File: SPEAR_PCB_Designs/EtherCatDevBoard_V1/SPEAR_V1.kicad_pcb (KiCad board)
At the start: 4 copper layers, 44 x 55 mm, 105 parts, among them J1 USB_C_Receptacle_USB2.0_16P, J2 FTSH-107-01-F-DV-K-P-TR, J3 Conn_01x21_Pin, J4 Conn_01x21_Pin, J5 SM04B-GHS-TB, J6 SM04B-GHS-TB, SW1 SW_Push, T1 H1102NLT, T2 H1102NLT, U1 USBLC6-2SC6, U2 STM32F446RCT6, U3 AMS1117-3.3, U4 LAN9252I/ML, U5 24FC512-I/SN, Y1 16MHz, Y2 25MHz

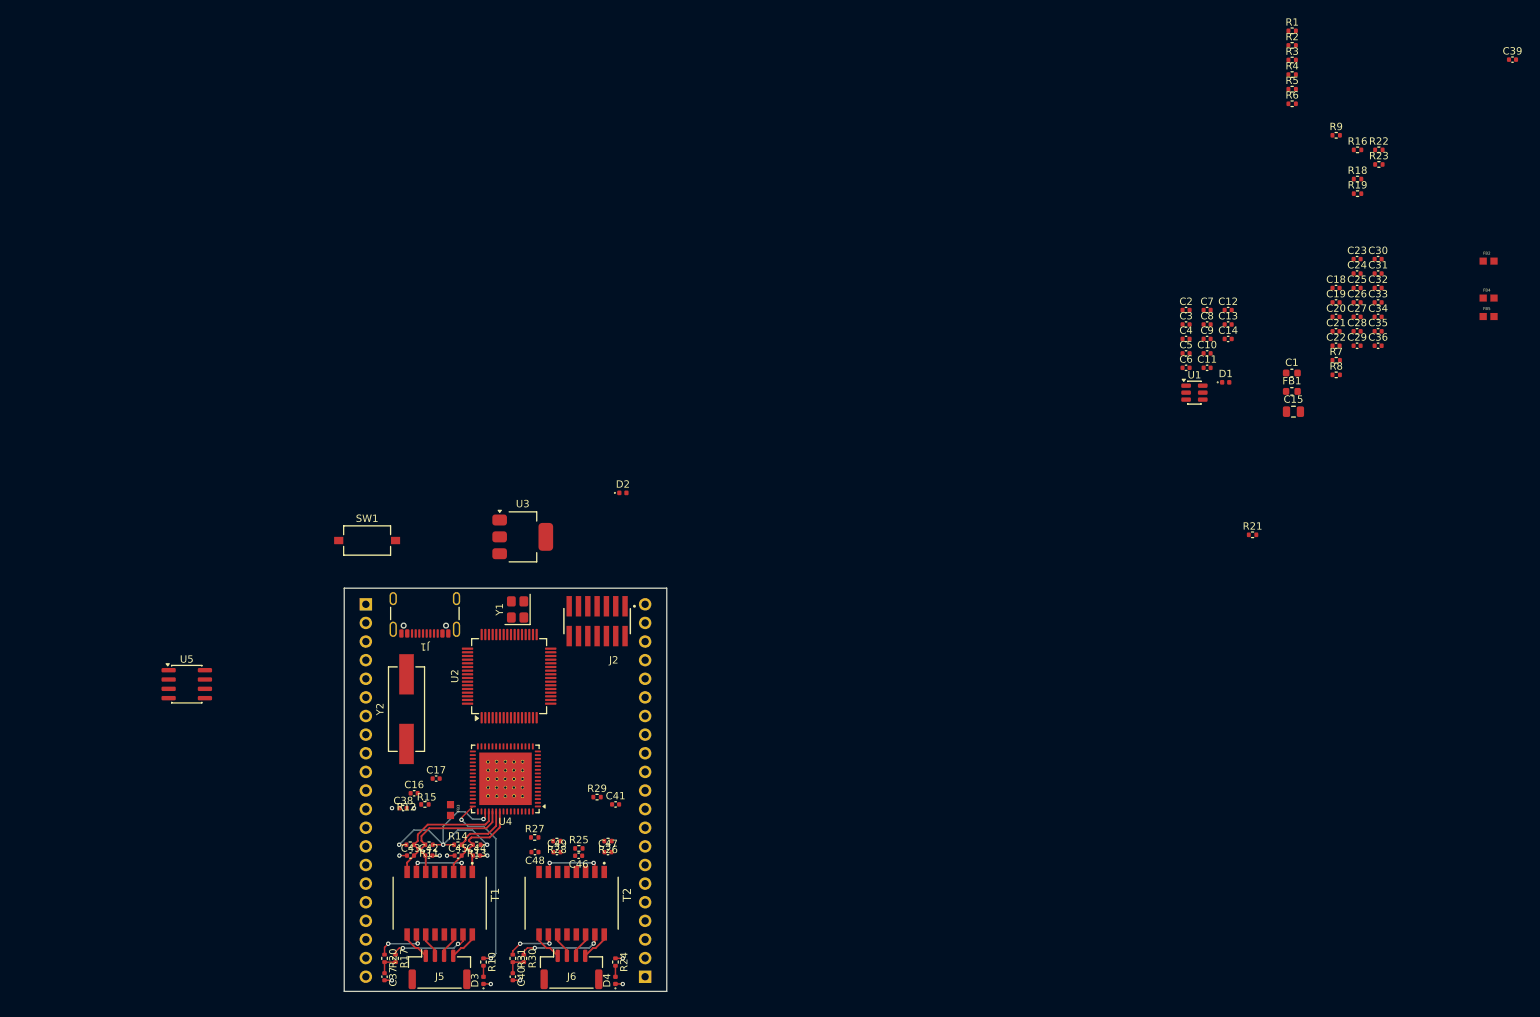
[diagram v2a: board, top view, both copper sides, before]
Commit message: Henry's continued work on the EtherCAT microcontroller dev. board.
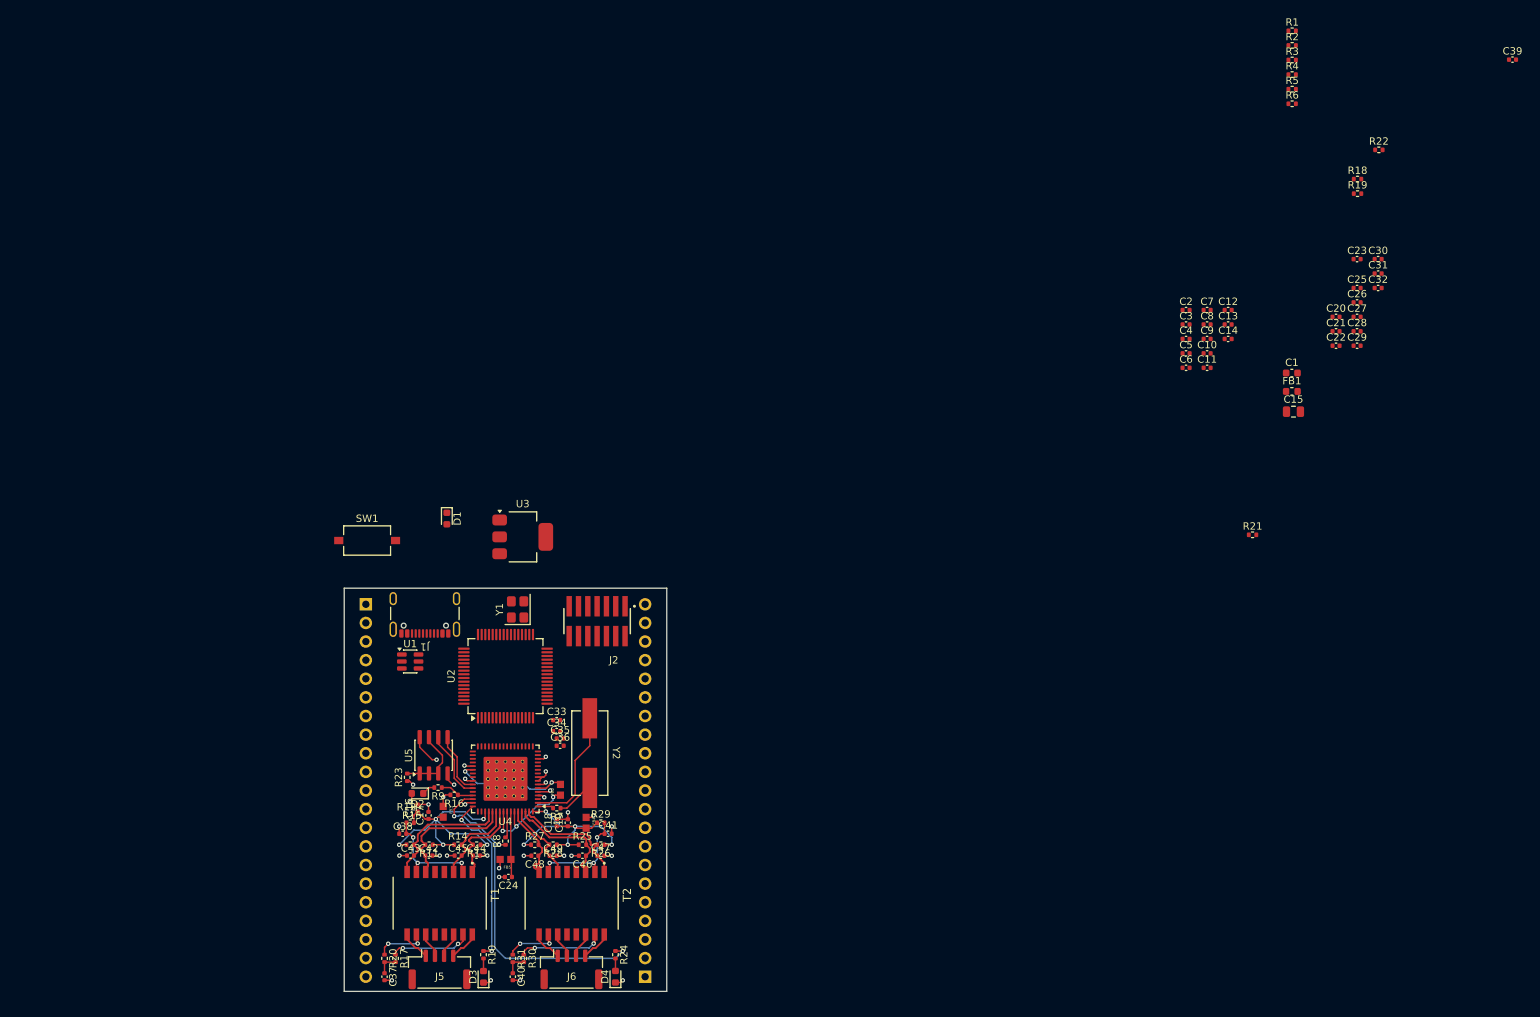
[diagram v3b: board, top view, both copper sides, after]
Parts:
- D1, D2, D3, D4: footprint LED_SMD:LED_0402_1005Metric -> LED_SMD:LED_0603_1608Metric
- moved R23 156.7 mm to (86.6, 127.8), turned to 90 degrees
- moved FB5 153.2 mm to (100.0, 139.0), turned to 180 degrees
- moved R9 151.4 mm to (90.8, 129.2), turned to 180 degrees
- moved R16 151.4 mm to (93.0, 130.2), turned to 180 degrees
- moved FB2 145.7 mm to (107.5, 129.5), turned to 90 degrees
- moved FB4 142.4 mm to (111.0, 134.0), turned to -90 degrees
- moved C24 142.1 mm to (100.4, 141.4), turned to 180 degrees
- moved R8 129.9 mm to (100.0, 136.5), turned to 90 degrees
- moved C18 128.9 mm to (107.0, 134.0), turned to 90 degrees
- moved C19 126.6 mm to (108.5, 134.0), turned to 90 degrees
- moved C33 125.7 mm to (107.0, 120.0)
- moved C34 125.5 mm to (107.0, 121.5)
- moved C35 124.6 mm to (107.5, 122.5)
- moved C36 124.2 mm to (107.5, 123.5)
- moved R7 122.6 mm to (107.0, 132.0), turned to 180 degrees
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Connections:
- C16 pad 2: Net-(C16-Pad2) -> GND
- C17 pad 2: Net-(C16-Pad2) -> GND
- C18 pad 2: Net-(C18-Pad2) -> GND
- C19 pad 2: Net-(C18-Pad2) -> GND
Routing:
- net /LAN9252/GPIO1: track 1.00 -> 45.0 mm, vias 1 -> 2
- net /LAN9252/VDD33TXRX2: track 0.00 -> 33.1 mm, vias 0 -> 5
- net GND: track 8.11 -> 29.2 mm, vias 9 -> 23
- net /LAN9252/VDDCR: track 0.00 -> 17.9 mm, vias 0 -> 2
- net +3.3V: track 0.00 -> 16.9 mm, vias 0 -> 10
- net Net-(U4-OSCO): track 0.00 -> 16.8 mm
- net /LAN9252/TXB_N: track 0.00 -> 16.4 mm
- net /LAN9252/TXB_P: track 0.00 -> 15.8 mm
- net /LAN9252/VDD12TX1: track 0.00 -> 15.0 mm, vias 0 -> 3
- net /LAN9252/RXB_N: track 0.00 -> 10.9 mm
- net /LAN9252/RXB_P: track 0.00 -> 10.8 mm
- net Net-(U5-A0): track 0.00 -> 10.2 mm
- net /LAN9252/I2C_SCL: track 0.00 -> 9.59 mm
- net Net-(U4-VDD33BIAS): track 0.00 -> 9.00 mm
- net /LAN9252/I2C_SDL: track 0.00 -> 8.52 mm
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
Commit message: Continued work on the pcb layout of the EtherCAT uC dev board. Updated schematic to use a power mux.
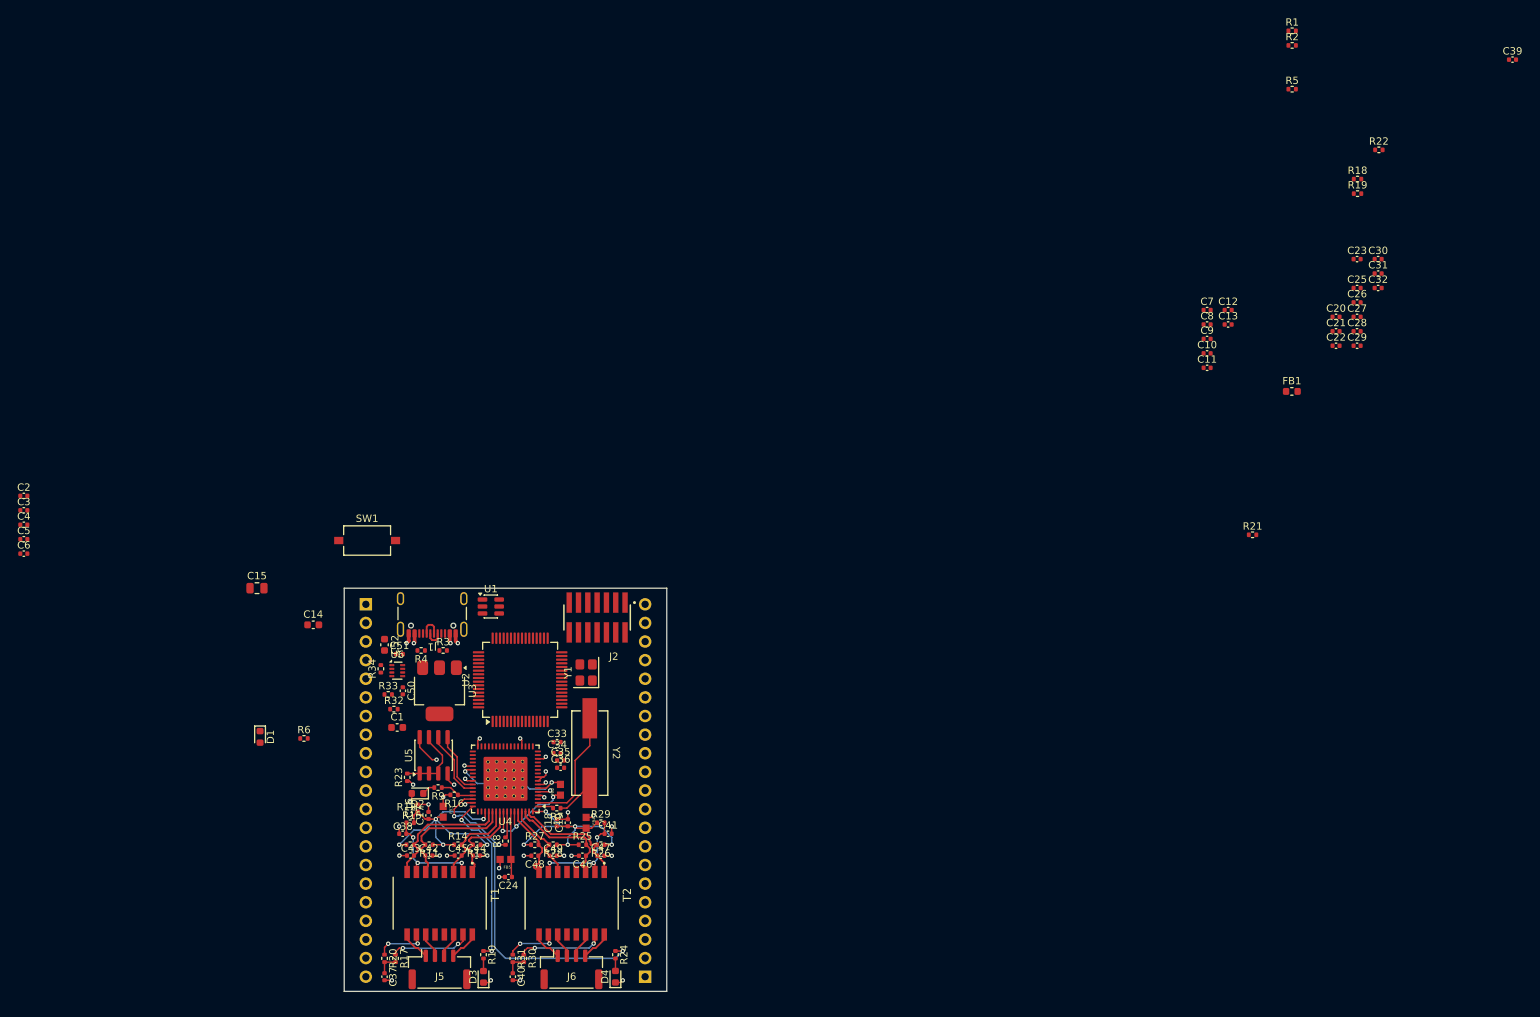
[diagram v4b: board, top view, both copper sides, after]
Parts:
- added C50: 1u, Capacitor_SMD:C_0402_1005Metric, F.Cu at (86.0, 116.0)
- added C51: 1u, Capacitor_SMD:C_0402_1005Metric, F.Cu at (85.5, 111.0)
- added C52: 10u, Capacitor_SMD:C_0603_1608Metric, F.Cu at (83.5, 109.7)
- added R32: 7.5k, Resistor_SMD:R_0402_1005Metric, F.Cu at (84.8, 118.5)
- added R33: 5.1k, Resistor_SMD:R_0402_1005Metric, F.Cu at (84.0, 116.5)
- added R34: 10k, Resistor_SMD:R_0402_1005Metric, F.Cu at (83.0, 113.0)
- added U6: TPS2116DRL, Package_TO_SOT_SMD:SOT-583-8, F.Cu at (85.2, 113.2)
- C14: footprint Capacitor_SMD:C_0402_1005Metric -> Capacitor_SMD:C_0603_1608Metric
- moved C2 160.6 mm to (34.3, 89.4)
- moved C3 160.6 mm to (34.3, 91.4)
- moved C4 160.6 mm to (34.3, 93.3)
- moved C5 160.6 mm to (34.3, 95.3)
- moved C6 160.6 mm to (34.3, 97.3)
- moved R6 160.2 mm to (72.5, 122.5)
- moved C15 143.4 mm to (66.1, 102.0)
- moved R4 142.4 mm to (88.5, 110.5), turned to 180 degrees
- moved R3 141.1 mm to (91.5, 110.5)
- moved C1 131.3 mm to (85.2, 121.0)
- moved C14 130.8 mm to (73.8, 107.0)
- moved D1 39.2 mm to (66.5, 122.3)
- moved U3 23.9 mm to (91.0, 116.0), turned to -90 degrees
- moved U1 13.3 mm to (98.0, 104.5)
- moved Y1 12.7 mm to (111.0, 113.5)
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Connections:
- C15 pad 1: +3.3V -> /STM32F446RC/3.3V_USB
- J3 pad 1: +3.3V -> /STM32F446RC/PC0
- J3 pad 10: /STM32F446RC/PA1 -> /STM32F446RC/PB0
- J3 pad 11: /STM32F446RC/PA4 -> /STM32F446RC/PB1
- J3 pad 12: /STM32F446RC/PC4 -> /STM32F446RC/PB2
- J3 pad 13: /STM32F446RC/PC5 -> /STM32F446RC/PB10
- J3 pad 14: /STM32F446RC/PB0 -> /STM32F446RC/PB12
- J3 pad 15: /STM32F446RC/PB1 -> /STM32F446RC/PB13
- J3 pad 16: /STM32F446RC/PB2 -> /STM32F446RC/PB14
- J3 pad 17: /STM32F446RC/PB10 -> /STM32F446RC/PB15
- J3 pad 18: /STM32F446RC/PB12 -> /STM32F446RC/PC9
- J3 pad 19: /STM32F446RC/PB13 -> /STM32F446RC/PC8
- J3 pad 2: +3.3V -> /STM32F446RC/PC1
- J3 pad 20: /STM32F446RC/PB14 -> /STM32F446RC/PC7
- J3 pad 21: /STM32F446RC/PB15 -> /STM32F446RC/PC6
- J3 pad 3: GND -> /STM32F446RC/PC2
- J3 pad 4: GND -> /STM32F446RC/PC3
- J3 pad 5: /STM32F446RC/PC0 -> /STM32F446RC/PA0
- J3 pad 6: /STM32F446RC/PC1 -> /STM32F446RC/PA1
- J3 pad 7: /STM32F446RC/PC2 -> /STM32F446RC/PA4
- J3 pad 8: /STM32F446RC/PC3 -> /STM32F446RC/PC4
- J3 pad 9: /STM32F446RC/PA0 -> /STM32F446RC/PC5
- J4 pad 1: /STM32F446RC/PC6 -> /STM32F446RC/3.3V_Battery
- J4 pad 2: /STM32F446RC/PC7 -> GND
- J4 pad 3: /STM32F446RC/PC8 -> +3.3V
- J4 pad 4: /STM32F446RC/PC9 -> GND
- U3 pad 2: +3.3V -> /STM32F446RC/3.3V_USB
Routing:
- net /STM32F446RC/USBC_D+: track 0.00 -> 3.07 mm
- net GND: track 29.2 -> 32.1 mm, vias 23 -> 25
- net +5V: track 0.00 -> 2.72 mm, vias 0 -> 2
- net /STM32F446RC/USBC_D-: track 0.00 -> 2.50 mm
- net +3.3V: track 16.9 -> 19.3 mm, vias 10 -> 12

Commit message: Edited schematic to fix problems with Lan9252. Continued work on pcb layout.
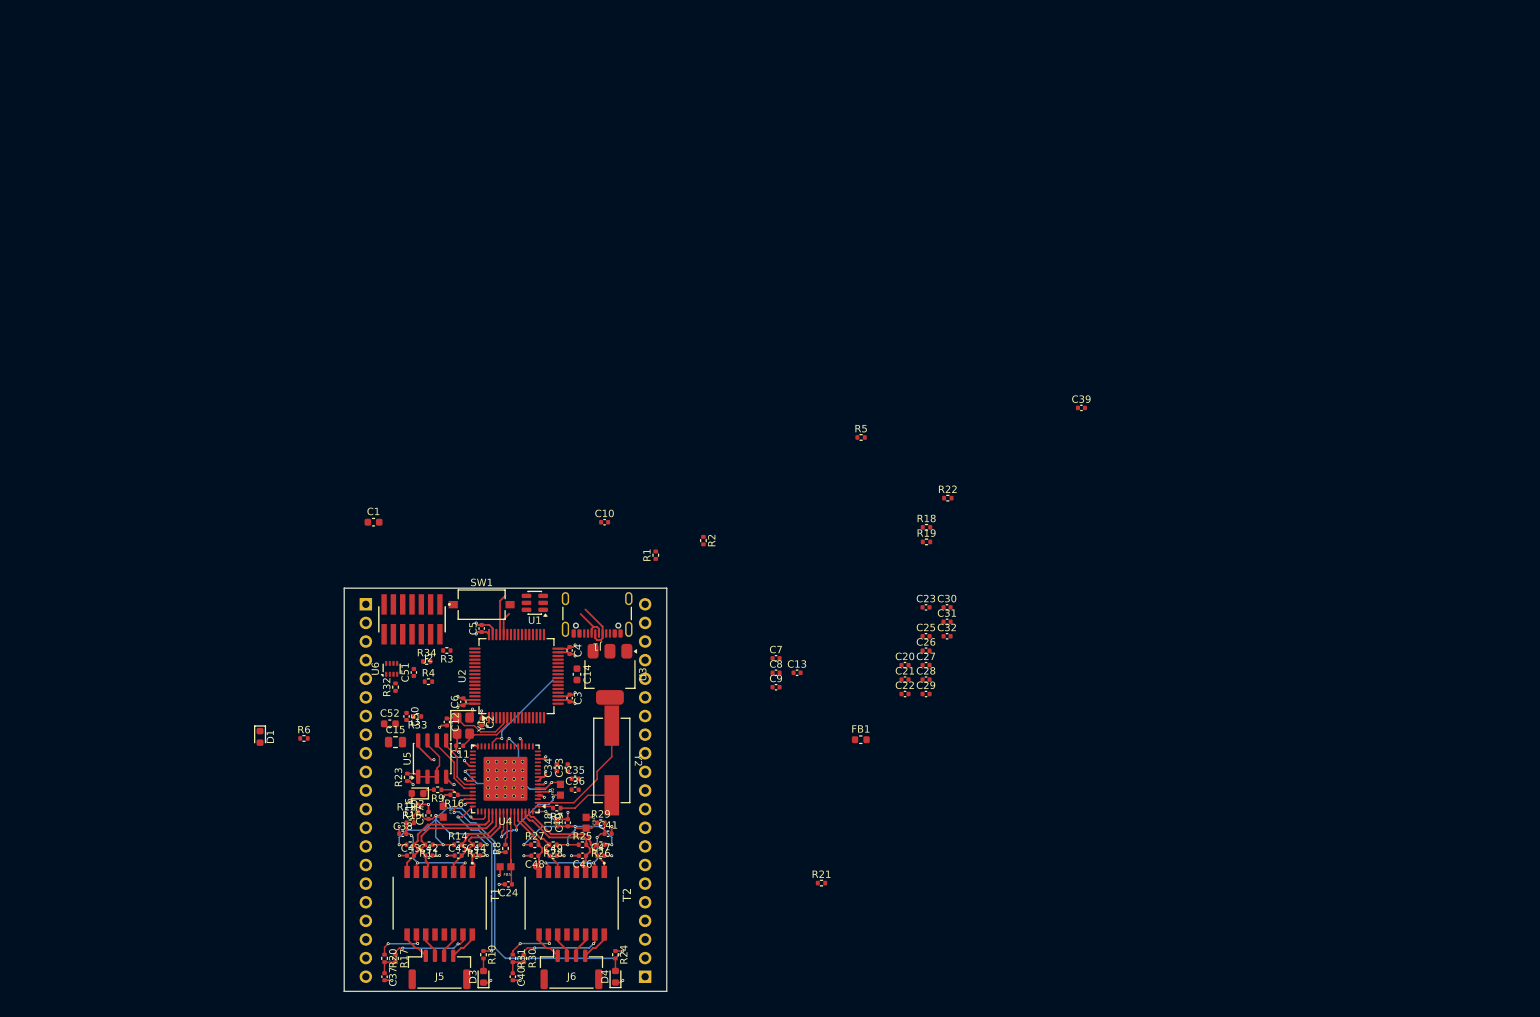
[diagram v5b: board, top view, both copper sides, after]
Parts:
- C33: value 0.1uF -> 1uF
- C34: value 0.1uF -> 470pF
- R6: value 5.1k -> 1k
- moved C12 120.5 mm to (92.0, 120.2), turned to -90 degrees
- moved C11 114.3 mm to (93.8, 123.5), turned to 180 degrees
- moved R1 112.5 mm to (120.5, 97.5), turned to 90 degrees
- moved R2 104.9 mm to (127.0, 95.5), turned to -90 degrees
- moved C10 85.4 mm to (113.5, 93.0)
- moved C3 78.7 mm to (108.8, 117.0), turned to -90 degrees
- moved C4 76.4 mm to (108.8, 110.5), turned to -90 degrees
- moved C13 75.6 mm to (139.8, 113.5)
- moved C20 75.6 mm to (154.5, 112.5)
- moved C21 75.6 mm to (154.5, 114.5)
- moved C8 75.6 mm to (136.9, 113.5)
- moved C9 75.6 mm to (136.9, 115.5)
- moved FB1 75.6 mm to (148.5, 122.7)
- moved C22 75.6 mm to (154.5, 116.4)
- moved C39 75.6 mm to (178.6, 77.4)
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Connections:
- J3 pad 8: /STM32F446RC/PC4 -> unconnected-(J3-Pin_8-Pad8)
- U2 pad 24: /STM32F446RC/PC4 -> /LAN9252/CS
- U4 pad 10: unconnected-(U4-FXSDB-Pad10) -> GND
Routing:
- net GND: track 32.1 -> 46.3 mm, vias 25 -> 31
- net /LAN9252/CS: track 0.00 -> 12.9 mm, vias 0 -> 1
- net +3.3V: track 19.3 -> 30.1 mm, vias 12 -> 17
- net /STM32F446RC/HSE_IN: track 0.00 -> 10.1 mm
- net /STM32F446RC/HSE_OUT: track 0.00 -> 8.55 mm
- net /LAN9252/VDDCR: track 17.9 -> 25.8 mm, vias 2 -> 3
- net /STM32F446RC/USB_D+: track 0.00 -> 5.64 mm
- net /STM32F446RC/USBC_D-: track 2.50 -> 6.75 mm
- net /STM32F446RC/USB_D-: track 0.00 -> 3.14 mm
- net +5V: track 2.72 -> 0.00 mm, vias 2 -> 0
- net Net-(C31-Pad2): track 5.13 -> 7.71 mm
- net /LAN9252/VDD12TX1: track 15.0 -> 17.1 mm
- net /LAN9252/VDD33TXRX1: track 37.9 -> 39.9 mm
- net /STM32F446RC/USBC_D+: track 3.07 -> 4.98 mm
- net Net-(U4-VDD33BIAS): track 9.00 -> 10.7 mm
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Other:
- board text added: "${REFERENCE}"
